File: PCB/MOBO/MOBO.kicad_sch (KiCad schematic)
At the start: 10 parts, among them J101 COMP_OUT, J102 COMP_5V, J103 COMP_GND, J104 RPi_GPio, J105 JST_02, J106 RPi_SDA0, J107 RPi_TV, J108 RPi_D-, J109 RPi_D+, J110 RPi_SCL0

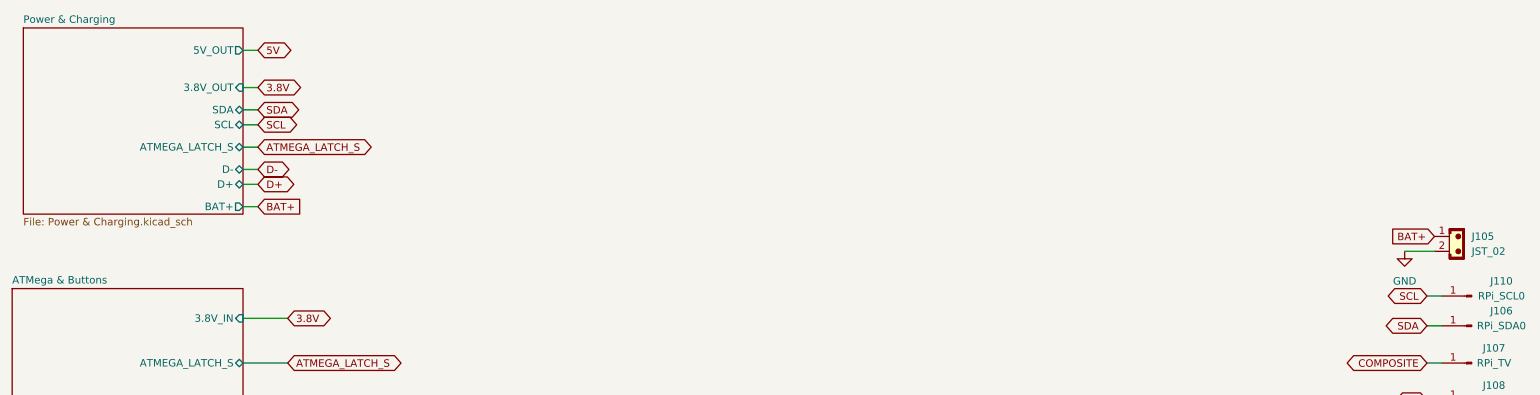
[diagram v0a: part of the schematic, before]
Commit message: fixed battery protection circuit
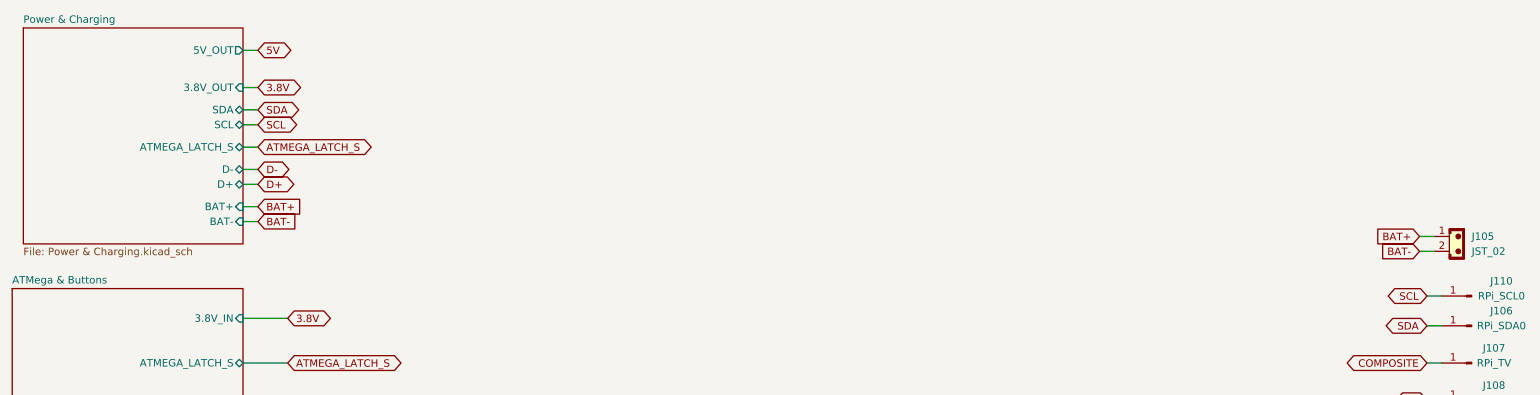
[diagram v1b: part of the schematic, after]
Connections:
- net GND: no longer J105.2
- new net BAT-: J105.2
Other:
- sheet Power & Charging ports: added BAT-; removed none
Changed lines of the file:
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@@
-    (stroke (width 0) (type default))
-  )
-  (wire (pts (xy 262.89 57.15) (xy 257.81 57.15))
     (stroke (width 0) (type default))
   )
@@
     (stroke (width 0) (type default))
   )
+  (wire (pts (xy 260.35 54.61) (xy 262.89 54.61))
+    (stroke (width 0) (type default))
+  )
   (wire (pts (xy 45.72 175.26) (xy 50.8 175.26))
     (stroke (width 0) (type default))
@@
     (stroke (width 0) (type default))
   )
+  (wire (pts (xy 59.69 52.07) (xy 62.23 52.07))
+    (stroke (width 0) (type default))
+  )
   (wire (pts (xy 264.16 82.55) (xy 261.62 82.55))
     (stroke (width 0) (type default))
@@
   )
   (wire (pts (xy 59.69 68.58) (xy 67.31 68.58))
+    (stroke (width 0) (type default))
+  )
+  (wire (pts (xy 262.89 57.15) (xy 260.35 57.15))
     (stroke (width 0) (type default))
   )
@@
     )
   )
-  (global_label "BAT+" (shape input) (at 262.89 54.61 180) (fields_autoplaced)
+  (global_label "BAT+" (shape input) (at 260.35 54.61 180) (fields_autoplaced)
     (effects (font (size 1.27 1.27)) (justify right))
-    (property "Intersheetrefs" "${INTERSHEET_REFS}" (at 255.0062 54.61 0)
+    (property "Intersheetrefs" "${INTERSHEET_REFS}" (at 252.4662 54.61 0)
       (effects (font (size 1.27 1.27)) (justify right) hide)
     )
@@
     )
   )
+  (global_label "BAT-" (shape input) (at 62.23 52.07 0) (fields_autoplaced)
+    (effects (font (size 1.27 1.27)) (justify left))
+    (property "Intersheetrefs" "${INTERSHEET_REFS}" (at 70.1138 52.07 0)
+      (effects (font (size 1.27 1.27)) (justify left) hide)
+    )
+  )
   (global_label "D-" (shape bidirectional) (at 62.23 43.18 0) (fields_autoplaced)
     (effects (font (size 1.27 1.27)) (justify left))
@@
     )
   )
+  (global_label "BAT-" (shape input) (at 260.35 57.15 180) (fields_autoplaced)
+    (effects (font (size 1.27 1.27)) (justify right))
+    (property "Intersheetrefs" "${INTERSHEET_REFS}" (at 252.4662 57.15 0)
+      (effects (font (size 1.27 1.27)) (justify right) hide)
+    )
+  )
   (global_label "D-" (shape bidirectional) (at 261.62 82.55 180) (fields_autoplaced)
     (effects (font (size 1.27 1.27)) (justify right))
@@
         (path "/2d62a3c1-c4f2-4921-9f6b-8dc8aef69d64"
           (reference "#FLG0102") (unit 1)
-        )
-      )
-    )
-  )
-  (symbol (lib_id "power:GND") (at 257.81 57.15 0) (mirror y) (unit 1)
-    (in_bom yes) (on_board yes) (dnp no) (fields_autoplaced)
-    (property "Reference" "#PWR0103" (at 257.81 63.5 0)
-      (effects (font (size 1.27 1.27)) hide)
-    )
-    (property "Value" "GND" (at 257.81 62.23 0)
-      (effects (font (size 1.27 1.27)))
-    )
-    (property "Footprint" "" (at 257.81 57.15 0)
-      (effects (font (size 1.27 1.27)) hide)
-    )
-    (property "Datasheet" "" (at 257.81 57.15 0)
-      (effects (font (size 1.27 1.27)) hide)
-    )
-    (pin "1")
-    (instances
-      (project "MOBO"
-        (path "/2d62a3c1-c4f2-4921-9f6b-8dc8aef69d64"
-          (reference "#PWR0103") (unit 1)
         )
       )
@@
     )
   )
-  (sheet (at 22.225 19.05) (size 37.465 31.75) (fields_autoplaced)
+  (sheet (at 22.225 19.05) (size 37.465 36.83) (fields_autoplaced)
     (stroke (width 0.1524) (type solid))
     (fill (color 0 0 0 0.0000))
@@
       (effects (font (size 1.27 1.27)) (justify left bottom))
     )
-    (property "Sheetfile" "Power & Charging.kicad_sch" (at 22.225 51.3846 0)
+    (property "Sheetfile" "Power & Charging.kicad_sch" (at 22.225 56.4646 0)
       (effects (font (size 1.27 1.27)) (justify left top))
     )
@@
       (effects (font (size 1.27 1.27)) (justify right))
     )
-    (pin "BAT+" output (at 59.69 49.53 0)
-      (effects (font (size 1.27 1.27)) (justify right))
-    )
+    (pin "BAT-" input (at 59.69 52.07 0)
+      (effects (font (size 1.27 1.27)) (justify right))
+    )
+    (pin "BAT+" input (at 59.69 49.53 0)
+      (effects (font (size 1.27 1.27)) (justify right))
+    )

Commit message: added usb esd ic and footprint
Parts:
- J104: footprint MountingHole:MountingHole_2.2mm_M2_DIN965_Pad -> Connector_PinHeader_2.00mm:PinHeader_2x20_P2.00mm_Vertical
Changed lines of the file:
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@@
       (effects (font (size 1.27 1.27)))
     )
-    (property "Footprint" "MountingHole:MountingHole_2.2mm_M2_DIN965_Pad" (at 265.43 123.19 0)
+    (property "Footprint" "Connector_PinHeader_2.00mm:PinHeader_2x20_P2.00mm_Vertical" (at 265.43 123.19 0)
       (effects (font (size 1.27 1.27)) hide)
     )
